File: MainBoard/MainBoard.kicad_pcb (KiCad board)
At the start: 4 copper layers, 35 x 35 mm, 115 parts, among them IC1 MAX30102, IC2 TESEO-LIV3F, J1 PV IN, J2 Conn_Coaxial, J3 Conn_01x30_Female, J4 RX, J5 RX, J6 Conn_01x04, J7 Conn_Coaxial, SW1 SW_DIP_x01, SW2 SW_DIP_x01, SW3 SW_DIP_x01, U1 BLUENRG-355MC, U2 MAX20361AEWC+, U3 STM32WL55CCU7, U4 LSM9DS1, U5 TPS63001, Y1 Crystal, Y2 Crystal, Y3 Crystal, Y4 Crystal

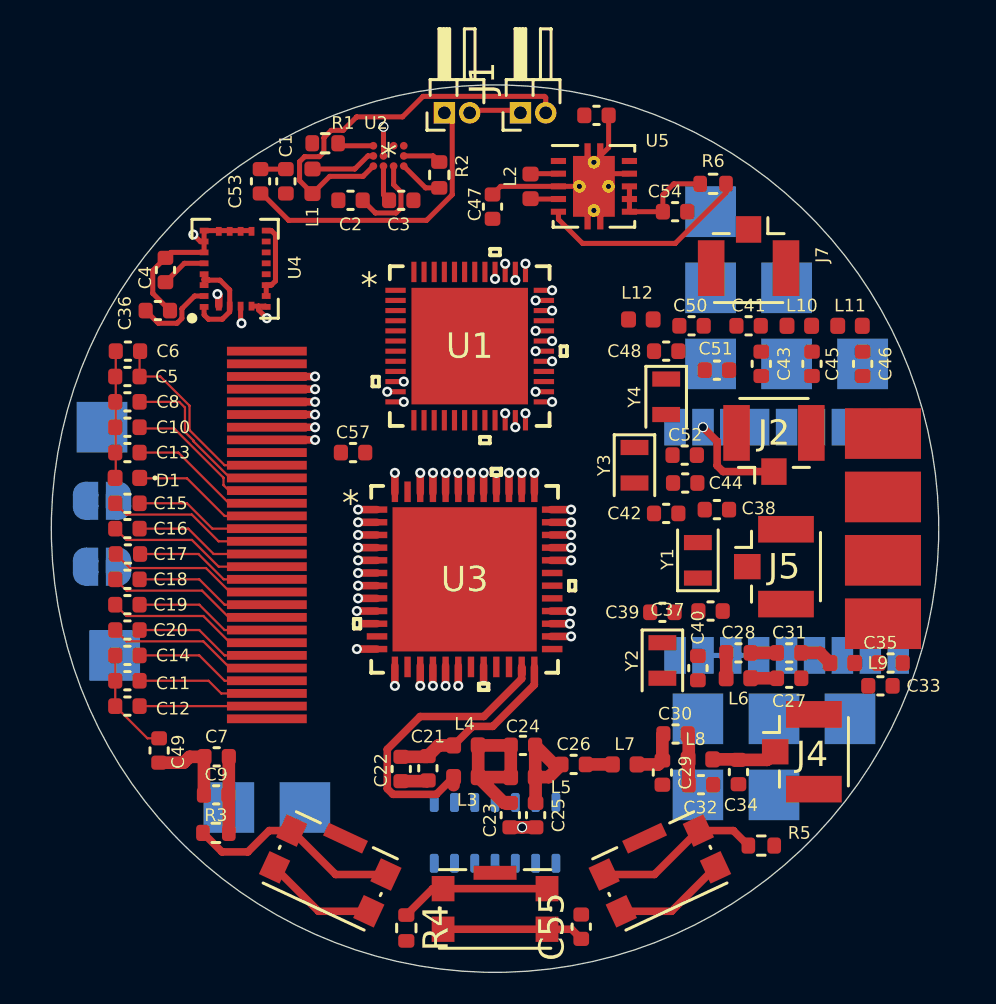
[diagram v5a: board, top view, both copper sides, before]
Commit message: ditch LoRa, switch processor to STM32WB30CE
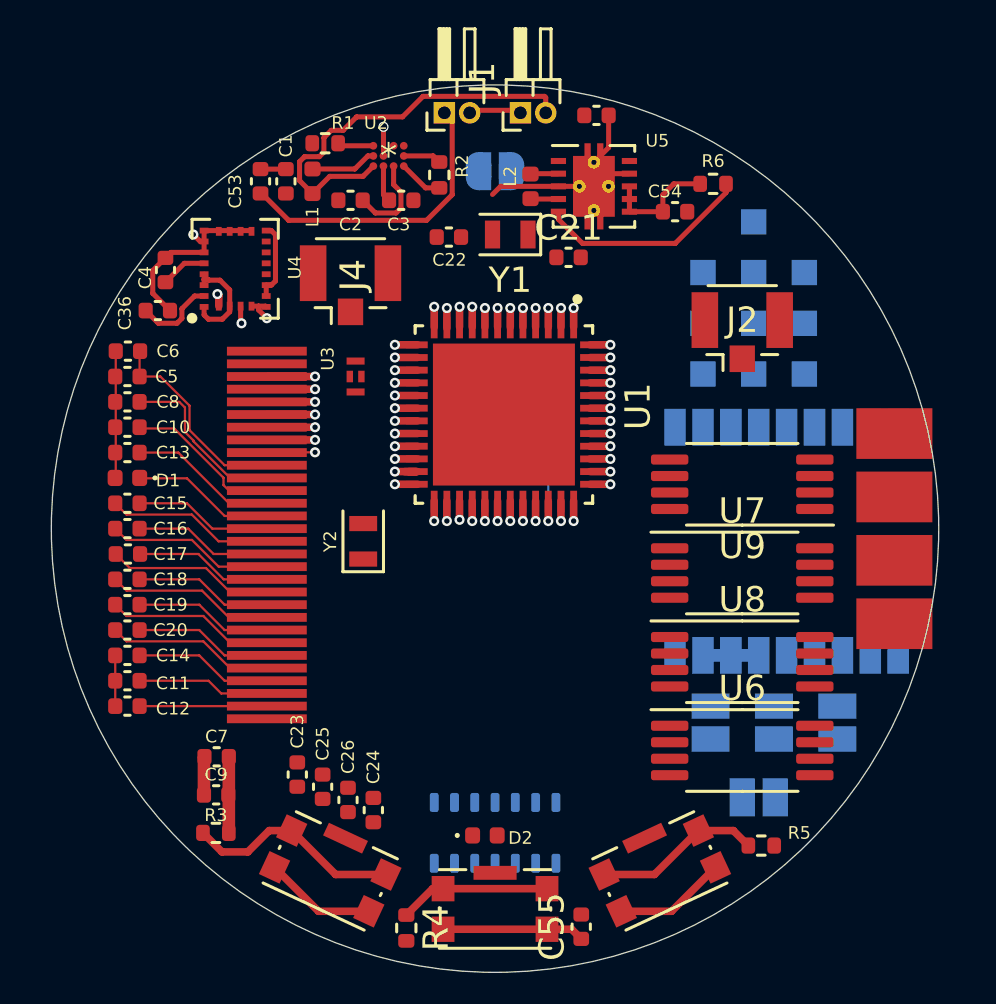
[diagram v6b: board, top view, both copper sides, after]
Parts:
- removed C27, C28, C29, C30, C31, C32, C33, C34, C35: 0.1uF, Capacitor_SMD:C_0402_1005Metric
- removed C37, C38, C39, C40, C41, C42, C43, C44, C45, C46, C47, C48, C49, C50, C51, C52, C57: _, Capacitor_SMD:C_0402_1005Metric
- removed J5: RX, Connector_Coaxial:U.FL_Hirose_U.FL-R-SMT-1_Vertical
- removed J7: Conn_Coaxial, Connector_Coaxial:U.FL_Hirose_U.FL-R-SMT-1_Vertical
- removed L10, L11, L12: _, Inductor_SMD:L_0402_1005Metric
- removed L3, L4, L5, L6, L7, L8, L9: 1uH, Inductor_SMD:L_0402_1005Metric
- removed TP12: RX, TestPoint:TestPoint_Pad_2.0x2.0mm
- removed TP13: TX, TestPoint:TestPoint_Pad_2.0x2.0mm
- removed TP15: BLE RSTN, TestPoint:TestPoint_Pad_2.0x2.0mm
- removed TP8: JTMS-SWDIO, TestPoint:TestPoint_Pad_2.0x2.0mm
- removed TP9: JTO-SWCLK, TestPoint:TestPoint_Pad_2.0x2.0mm
- removed Y3, Y4: Crystal, Crystal:Crystal_SMD_2012-2Pin_2.0x1.2mm
- added D2: 1.8V, Diode_SMD:D_0402_1005Metric, F.Cu at (134.1, 47.1)
- added JP3: WP3, Jumper:SolderJumper-2_P1.3mm_Open_Pad1.0x1.5mm, B.Cu at (143.0, 42.6)
- added JP4: WP2, Jumper:SolderJumper-2_P1.3mm_Open_Pad1.0x1.5mm, B.Cu at (145.5, 42.6)
- added JP5: WP4, Jumper:SolderJumper-2_P1.3mm_Open_Pad1.0x1.5mm, B.Cu at (144.9, 45.6)
- added U6: CAT24M01Y, Package_SO:TSSOP-8_4.4x3mm_P0.65mm, F.Cu at (144.2, 43.8)
- added U7: CAT24M01Y, Package_SO:TSSOP-8_4.4x3mm_P0.65mm, F.Cu at (144.2, 36.8)
- added U8: CAT24M01Y, Package_SO:TSSOP-8_4.4x3mm_P0.65mm, F.Cu at (144.2, 40.2)
- added U9: CAT24M01Y, Package_SO:TSSOP-8_4.4x3mm_P0.65mm, F.Cu at (144.2, 33.2)
- C21, C22: value 0.1uF -> Loading
- C23: value 0.1uF -> 1pF
- C24: value 0.1uF -> 10pF
- C25: value 0.1uF -> 100pF
- C26: value 0.1uF -> 1mF
- J4: value RX -> Conn_Coaxial
- JP2: value PV EN -> WP1; footprint Jumper:SolderJumper-2_P1.3mm_Open_RoundedPad1.0x1.5mm -> Jumper:SolderJumper-2_P1.3mm_Open_Pad1.0x1.5mm
- TP1: value NRST -> TestPoint; footprint TestPoint:TestPoint_Pad_2.0x2.0mm -> TestPoint:TestPoint_Pad_1.0x1.0mm
- TP10, TP11, TP14: footprint TestPoint:TestPoint_Pad_2.0x2.0mm -> TestPoint:TestPoint_Pad_1.0x1.0mm
- TP2: value JTRST -> JTMS_SWDIO; footprint TestPoint:TestPoint_Pad_2.0x2.0mm -> TestPoint:TestPoint_Pad_1.0x1.0mm
- TP3: value BLE TX -> JTCK_SWCLK; footprint TestPoint:TestPoint_Pad_2.0x2.0mm -> TestPoint:TestPoint_Pad_1.0x1.0mm
- TP4: value JTO-SWO -> JTDI; footprint TestPoint:TestPoint_Pad_2.0x2.0mm -> TestPoint:TestPoint_Pad_1.0x1.0mm
- TP5: value PA10 -> JTDO; footprint TestPoint:TestPoint_Pad_2.0x2.0mm -> TestPoint:TestPoint_Pad_1.0x1.0mm
- TP6: value BLE RX -> NJTRST; footprint TestPoint:TestPoint_Pad_2.0x2.0mm -> TestPoint:TestPoint_Pad_1.0x1.0mm
- TP7: value JTCK-SWDIO -> BOOT0; footprint TestPoint:TestPoint_Pad_2.0x2.0mm -> TestPoint:TestPoint_Pad_1.0x1.0mm
- U1: value BLUENRG-355MC -> STM32WB30CEU5A; footprint libs:BLUENRG -> libs:STM32WB30CEU5A
- U3: value STM32WL55CCU7 -> DLF162500LT-5028A1; footprint libs:STM32WL55CCU7 -> libs:DLF162500LT
- Y1: value Crystal -> 32 kHz
- Y2: value Crystal -> 32 MHz
- moved JP2 30.3 mm to (148.0, 42.6), turned to 90 degrees
- moved TP3 28.4 mm to (146.7, 24.9)
- moved TP6 28.2 mm to (142.7, 24.9)
- moved TP5 27.5 mm to (144.7, 24.9)
- moved J4 25.6 mm to (128.8, 25.4), turned to 90 degrees
- moved JP1 22.0 mm to (134.5, 20.9), turned to 0 degrees
- moved C22 21.1 mm to (132.7, 23.5), turned to 180 degrees
- moved C21 20.9 mm to (137.4, 24.3), turned to 0 degrees
- moved TP7 19.7 mm to (144.7, 22.9)
- moved TP14 16.7 mm to (144.7, 28.9)
- moved Y1 14.8 mm to (135.1, 23.4), turned to 180 degrees
- moved Y2 12.7 mm to (129.3, 35.5), turned to 90 degrees
- moved U3 9.08 mm to (129.0, 29.0), turned to 90 degrees
- moved C26 9.01 mm to (128.7, 45.7), turned to 90 degrees
- moved C23 8.55 mm to (126.7, 44.7), turned to 90 degrees
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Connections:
- C21 pad 1: VR_PA -> Net-(C21-Pad1)
- C22 pad 1: VR_PA -> Net-(C22-Pad1)
- C23 pad 1: Net-(C23-Pad1) -> +3V3
- C24 pad 1: Net-(C23-Pad1) -> +3V3
- C24 pad 2: Net-(C24-Pad2) -> GND
- C25 pad 1: Net-(C24-Pad2) -> +3V3
- C26 pad 1: Net-(C24-Pad2) -> +3V3
- C26 pad 2: Net-(C26-Pad2) -> GND
- IC1 pad 11: (no net) -> Net-(D2-Pad2)
- IC2 pad 2: RX1 -> RX
- IC2 pad 3: TX1 -> TX
- J4 pad 1: Net-(C34-Pad1) -> Net-(J4-Pad1)
- JP2 pad 1: (no net) -> Net-(JP2-Pad1)
- JP2 pad 2: Net-(JP2-Pad2) -> +3V3
- U1 pad 1: (no net) -> +3V3
- U1 pad 10: Net-(TP5-Pad1) -> SPI1-SCK
- U1 pad 11: Net-(TP3-Pad1) -> Net-(IC2-Pad4)
- U1 pad 12: Net-(TP6-Pad1) -> Net-(IC2-Pad5)
- U1 pad 15: (no net) -> Net-(J3-Pad9)
- U1 pad 16: (no net) -> SPI1-MOSI
- U1 pad 17: (no net) -> Net-(J3-Pad8)
- U1 pad 18: (no net) -> TX
- U1 pad 19: (no net) -> Net-(J3-Pad7)
- U1 pad 2: (no net) -> Net-(C21-Pad1)
- U1 pad 20: (no net) -> +3V3
- U1 pad 21: (no net) -> Net-(U1-Pad21)
- U1 pad 22: Net-(C41-Pad2) -> GND
- U1 pad 24: Net-(C42-Pad1) -> Net-(U1-Pad24)
- U1 pad 25: Net-(C44-Pad1) -> Net-(U1-Pad25)
- U1 pad 26: +3V3 -> (no net)
- U1 pad 28: (no net) -> Net-(J3-Pad5)
- U1 pad 29: Net-(C52-Pad1) -> Net-(J3-Pad6)
- U1 pad 3: (no net) -> Net-(C22-Pad1)
- U1 pad 30: Net-(C51-Pad1) -> (no net)
- U1 pad 31: Net-(C48-Pad1) -> +3V3
- U1 pad 32: Net-(C50-Pad1) -> GND
- U1 pad 33: (no net) -> +3V3
- U1 pad 34: GND -> +3V3
- U1 pad 35: Net-(L12-Pad1) -> +3V3
- U1 pad 36: +3V3 -> RX
- U1 pad 37: +3V3 -> (no net)
- U1 pad 38: Net-(TP15-Pad1) -> (no net)
- U1 pad 39: +3V3 -> Net-(TP2-Pad1)
- U1 pad 4: (no net) -> Net-(TP7-Pad1)
- U1 pad 40: Net-(C47-Pad1) -> +3V3
- U1 pad 41: (no net) -> Net-(TP3-Pad1)
- U1 pad 42: (no net) -> Net-(TP4-Pad1)
- U1 pad 43: (no net) -> Net-(TP5-Pad1)
- U1 pad 44: (no net) -> Net-(TP6-Pad1)
- U1 pad 45: (no net) -> Net-(R5-Pad1)
- U1 pad 46: (no net) -> Net-(R4-Pad1)
- U1 pad 47: (no net) -> Net-(R3-Pad1)
- U1 pad 48: (no net) -> +3V3
- U1 pad 49: (no net) -> GND
- U1 pad 5: (no net) -> SCL
- U1 pad 6: (no net) -> SDA
- U1 pad 7: (no net) -> Net-(TP1-Pad1)
- U1 pad 8: (no net) -> +3V3
- U1 pad 9: (no net) -> Net-(BT1-Pad1)
- U3 pad 1: Net-(TP4-Pad1) -> Net-(U1-Pad21)
- U3 pad 2: Net-(TP2-Pad1) -> GND
- U3 pad 3: SPI1-MOSI -> Net-(J4-Pad1)
- U3 pad 4: SCL -> GND
- Y1 pad 1: Net-(C37-Pad1) -> Net-(C21-Pad1)
- Y1 pad 2: Net-(C38-Pad1) -> Net-(C22-Pad1)
- Y2 pad 1: Net-(C39-Pad1) -> Net-(U1-Pad25)
- Y2 pad 2: Net-(C40-Pad1) -> Net-(U1-Pad24)
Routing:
- net RFO_HP: track 12.1 -> 0.00 mm
- net Net-(J3-Pad9): track 0.80 -> 10.5 mm, vias 1 -> 2
- net +3V3: track 31.2 -> 39.4 mm
- net VR_PA: track 7.16 -> 0.00 mm
- net Net-(C23-Pad1): track 6.78 -> 0.00 mm
- net (no net): track 0.00 -> 5.57 mm, vias 0 -> 7
- net Net-(C24-Pad2): track 4.89 -> 0.00 mm
- net Net-(IC2-Pad11): track 4.09 -> 0.00 mm, vias 1 -> 0
- net GND: track 38.2 -> 34.7 mm, vias 6 -> 5
- net Net-(C30-Pad2): track 3.03 -> 0.00 mm
- net Net-(C34-Pad1): track 2.61 -> 0.00 mm
- net Net-(C29-Pad1): track 2.12 -> 0.00 mm
- net RFI_P: track 1.80 -> 0.00 mm, vias 1 -> 0
- net Net-(C31-Pad2): track 1.30 -> 0.00 mm
- net Net-(J3-Pad7): track 10.0 -> 11.1 mm
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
